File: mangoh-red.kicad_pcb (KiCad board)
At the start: 6 copper layers, 70 x 61.8 mm, 590 parts, among them CN1000 uFL, CN301 uFL, CN302 uFL, CN303 uFL, CN304 USB_A, CN305 USB_B_Micro, CN306 Conn_02x19_Counter_Clockwise, CN307 Conn_02x13_Odd_Even, CN310 Conn_02x03_Odd_Even, CN312 Conn_02x03_Odd_Even, CN400 Conn_02x05_Odd_Even, CN401 Conn_02x05_Odd_Even, CN500 JP036-RT3B4AB, CN801 USB_B_Micro, CN802 Conn_01x02, CN804 Conn_01x03, J200 CF3-Socket, Q312 NSBC114YDP6T5G, Q400 NSBC114YDP6T5G, Q405 NSBC114YDP6T5G, Q600 PDTC115EM, SW401 Conn_02x08_Counter_Clockwise, U1000 MT7697, U1001 MX25L3233FM1I-08G_TR, U1004 SX1509BIULTRT, U1005 TPS61253YFFR, U1006 CP2130-F01-GM, U1007 24AA32AF-I-MNY, U1010 74LVC2G126HD4-7, U1020 74LVC2G126HD4-7, U301 FT230XQ-R, U302 TS3A5018RSVR, U304 74LVC2G126HD4-7, U306 FXMA108BQX, U307 FXMA108BQX, U337 FXMA108BQX, U400 NCP303LSN30T1G, U401 74AUP1G08GM, U402 74AUP1G08GM, U404 TCA9546APWR, U405 74AUP1G08GM, U500 WM8944BECS_R, U501 TS3A5018RSVR, U600 XC6223H29B9R-G, U610 TXS02612ZQSR, U701 USB3503A-1-GL-TR, U702 MIC2026-1YM, U704 BMI160, U705 BMP280, U706 PNJ4K01F, U800 BQ24296RGER, U801 LTC2942IDCB_TRMPBF, U900 TPS7A7300, U901 TPS62420DRC, U903 XC6221A182MR, Y1000 CT2520DB26000C0FZZA1

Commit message: Update
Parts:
- added CN600: CN600, MangOH-Red:CONN_25P_1780x1290_0088CC_MICROSDSIM, B.Cu at (127.6, 74.2)
- added FIL1000: BL1608-05A2450TB, MangOH-Red:FIL_6P_0160x0080_0050CC_MURATA, F.Cu at (203.7, 60.6)
- added L1000: 2.2u, Inductor_SMD:L_0603_1608Metric_Pad1.05x0.95mm_HandSolder, F.Cu at (195.0, 76.7)
- added OSC700: ENE3687A, Crystal:Crystal_SMD_SeikoEpson_FA238V-4Pin_3.2x2.5mm, F.Cu at (211.7, 75.5)
- added SW200: PTS810, Button_Switch_SMD:SW_SPST_PTS810, F.Cu at (212.4, 67.4)
- added SW400: SKTDLDE010, Button_Switch_SMD:SW_SPST_EVQP7A, F.Cu at (196.1, 67.2)
- added SW402: SKTDLDE010, Button_Switch_SMD:SW_SPST_EVQP7A, F.Cu at (202.7, 67.2)
- added U603: ESIM, MangOH-Red:DFN_8P_0500x0600_SLUG_0420x0340_0127CC_ESIM_MODULE_MFF2, F.Cu at (194.4, 60.9)
- SW401: footprint Button_Switch_SMD:SW_DIP_SPSTx08_Slide_6.7x21.88mm_W6.73mm_P2.54mm_LowProfile_JPin -> Button_Switch_SMD:SW_DIP_SPSTx08_Slide_Omron_A6H-8101_W6.15mm_P1.27mm
- U900: footprint Package_DFN_QFN:QFN-20-1EP_5x5mm_P0.65mm_EP3.35x3.35mm -> MangOH-Red:QFN_20P_0500x0500_SLUG_0320x0320_0065CC
- moved D302 147.9 mm to (124.6, 97.8), turned to 90 degrees
- moved L300 143.2 mm to (134.0, 107.0)
- moved TP907 141.5 mm to (146.3, 77.3)
- moved R310 139.7 mm to (134.5, 71.2), turned to 270 degrees
- moved D303 139.7 mm to (134.0, 108.0)
- moved R311 137.1 mm to (135.4, 71.2), turned to 270 degrees
- moved TP261 135.5 mm to (130.2, 93.9)
- moved TP232 134.7 mm to (131.0, 91.2), turned to 270 degrees
- moved D301 132.1 mm to (141.6, 108.0)
- moved TP901 130.2 mm to (156.8, 68.8)
- moved D400 128.5 mm to (125.7, 60.1)
- moved TP906 128.5 mm to (157.7, 76.9)
- moved R506 128.4 mm to (144.6, 57.4), turned to 90 degrees
- moved TP903 128.0 mm to (148.6, 91.1)
- moved TP500 127.2 mm to (160.2, 63.0), turned to 270 degrees
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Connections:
- J200 pad 57: (no net) -> UIM2_RST
- R611 pad 2: (no net) -> Net-(R611-Pad2)
- R645 pad 1: (no net) -> Net-(R645-Pad1)
- U1000 pad 40: (no net) -> Net-(L1000-Pad1)
- U701 pad B3: (no net) -> Net-(OSC700-Pad3)

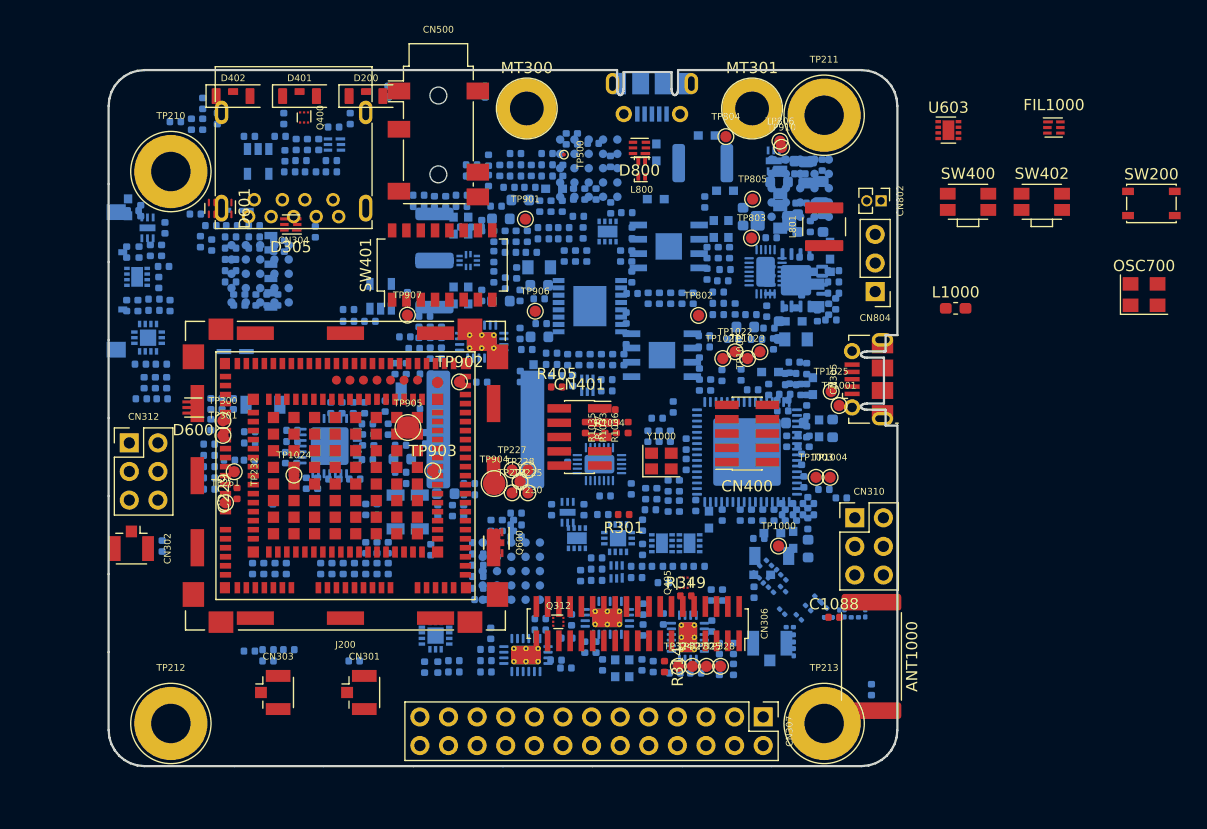
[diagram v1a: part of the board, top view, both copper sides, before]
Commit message: Update models and parts placement
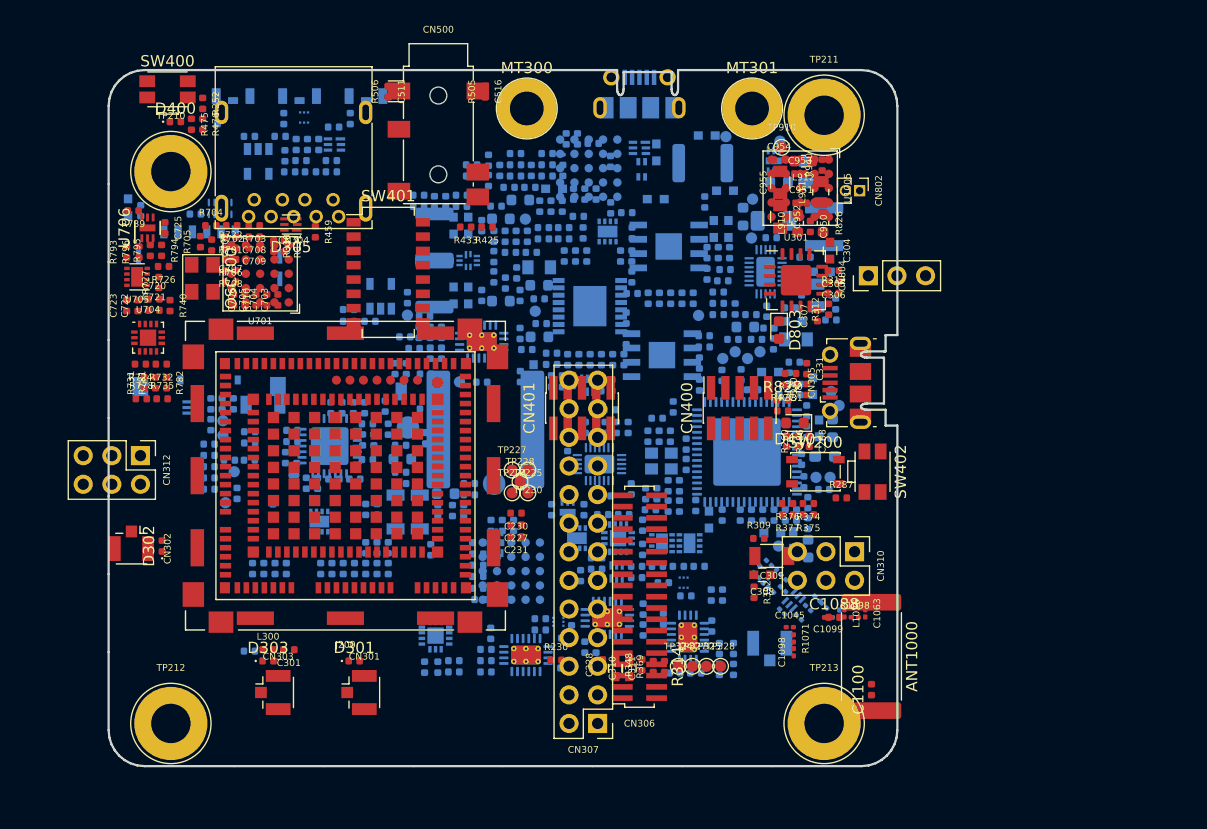
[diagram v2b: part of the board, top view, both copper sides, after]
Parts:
- C1045, C1063, C1098, C1099, C1100, C227, C228, C230, C231, C288, C301, C304, C305, C306, C307, C308, C309, C310, C311, C330, C331, C511, C516, C702, C703, C704, C705, C706, C707, C708, C709, C720, C721, C722, C723, C725, C950, C951, C952, C953, C954, C955, D301, D302, D303, D400, D410, D803, L1026, L300, L910, L911, L912, R1071, R1098, R230, R252, R260, R286, R287, R309, R310, R311, R312, R313, R330, R331, R348, R369, R374, R375, R376, R377, R392, R425, R433, R459, R475, R476, R477, R505, R506, R701, R702, R703, R704, R705, R706, R708, R710, R722, R724, R726, R727, R731, R732, R735, R739, R740, R778, R781, R782, R793, R794, R795, R796, R822, R826, R940, U1005, U301, U701, U704, U705, U706: moved to F.Cu
- C229, D200, D401, D402, D600, D601, D800, FIL1000, L1000, L800, L801, Q312, Q400, Q405, Q600, R1033, R1034, R1035, R1036, R301, R349, R405, R777, TP1000, TP1001, TP1002, TP1003, TP1004, TP1021, TP1022, TP1023, TP1024, TP1025, TP232, TP261, TP300, TP301, TP500, TP802, TP803, TP804, TP805, TP806, TP901, TP902, TP903, TP904, TP905, TP906, TP907, U603, Y1000: moved to B.Cu
- moved OSC700 83.6 mm to (128.1, 74.0), turned to 270 degrees
- moved SW400 71.8 mm to (125.0, 57.2)
- moved U603 65.8 mm to (138.5, 95.6), turned to 90 degrees
- moved FIL1000 47.9 mm to (180.6, 102.6), turned to 45 degrees
- moved SW200 38.2 mm to (182.6, 91.2)
- moved SW402 28.3 mm to (187.6, 91.2), turned to 270 degrees
- moved L1000 17.5 mm to (183.4, 89.8), turned to 180 degrees
- moved CN307 14.7 mm to (163.2, 113.5), turned to 180 degrees
- moved SW401 4.83 mm to (144.6, 73.5), turned to 0 degrees
- moved CN310 3.01 mm to (186.0, 98.3), turned to 270 degrees
- moved CN401 2.58 mm to (161.8, 85.5), turned to 90 degrees
- moved CN600 2.54 mm to (128.7, 76.5), turned to 180 degrees
- moved CN306 2.39 mm to (166.9, 102.3), turned to 180 degrees
- moved CN400 2.35 mm to (175.8, 85.5), turned to 90 degrees
- moved CN802 2.10 mm to (186.5, 66.2)
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
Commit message: Update
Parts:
- moved CN307 14.9 mm to (178.1, 113.3), turned to 270 degrees
- moved ANT1000 6.32 mm to (193.8, 108.0)
- moved CN310 2.46 mm to (185.4, 95.9), turned to 0 degrees
- moved CN802 1.81 mm to (187.8, 65.0), turned to 0 degrees
- moved CN304 1.70 mm to (139.7, 65.3)
- moved CN312 1.60 mm to (121.7, 88.4), turned to 0 degrees
- moved CN306 1.32 mm to (166.1, 103.3), turned to 270 degrees
- moved CN804 0.97 mm to (187.7, 74.6), turned to 180 degrees
- moved SW401 0.60 mm to (145.2, 73.4), turned to 90 degrees
- turned CN600 to 90 degrees

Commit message: Update
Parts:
- CN304: footprint Connector_USB:USB3_A_Molex_48393-001 -> MangOH-Red:CONN_4P_1450x1400_USB_2GND_RA_THRU
- CN306: footprint Connector_PinSocket_1.00mm:PinSocket_2x19_P1.00mm_Vertical_SMD -> MangOH-Red:CONN_38P_1820x1150_0080CC_EVERCLEAR
- CN307: footprint Connector_PinHeader_2.54mm:PinHeader_2x13_P2.54mm_Vertical -> MangOH-Red:CONN_26P_3300x0483_0254CC_HEADER_THRU
- CN310, CN312: footprint Connector_PinHeader_2.54mm:PinHeader_2x03_P2.54mm_Vertical -> MangOH-Red:CONN_6P_0760x0510_HEADER_THRU_0254CC
- CN400, CN401: footprint Connector_PinSocket_1.27mm:PinSocket_2x05_P1.27mm_Vertical_SMD -> MangOH-Red:CONN_10P_0673x0305_0127CC_SMT
- CN801: footprint Connector_USB:USB_Micro-B_Molex-105017-0001 -> MangOH-Red:CONN_5P_0750x0560_USB_5GND_HRS_ZX62RD
- CN802: footprint Connector_PinHeader_1.27mm:PinHeader_1x02_P1.27mm_Vertical -> MangOH-Red:CONN_2P_0590x0450_0200CC_THRU_HEADER
- CN804: footprint Connector_PinHeader_2.54mm:PinHeader_1x03_P2.54mm_Vertical -> MangOH-Red:CONN_3P_0762x0254_VERTICAL_HEADER_SINGLE_ROW_THRU_SAMTEC_TSW
- SW401: footprint Button_Switch_SMD:SW_DIP_SPSTx08_Slide_Omron_A6H-8101_W6.15mm_P1.27mm -> MangOH-Red:SW_16P_1128x0620_0127CC_DIP_SPST
- moved CN307 14.7 mm to (163.4, 113.3), turned to 180 degrees
- moved ANT1000 4.25 mm to (197.8, 106.6)
- moved CN310 2.29 mm to (186.2, 98.0), turned to 270 degrees
- moved CN306 1.61 mm to (167.1, 102.0), turned to 180 degrees
- moved CN312 1.53 mm to (122.8, 89.5), turned to 270 degrees
- moved CN802 1.53 mm to (186.7, 66.0), turned to 270 degrees
- moved CN304 1.48 mm to (139.9, 66.8)
- moved CN804 1.12 mm to (187.4, 73.5), turned to 90 degrees
- moved SW401 0.47 mm to (144.8, 73.2), turned to 0 degrees
- moved C1000 0.29 mm to (168.7, 86.2)
- moved C1006 0.29 mm to (177.2, 83.7)
- moved C1015 0.29 mm to (182.1, 93.7)
- moved C1020 0.29 mm to (178.1, 94.8)
- moved C1021 0.29 mm to (169.7, 94.0)
- moved C1024 0.29 mm to (173.3, 95.2)
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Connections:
- J200 pad 27: (no net) -> UIM1_CLK
- J200 pad 29: (no net) -> UIM1_RESET
- R600 pad 2: (no net) -> Net-(CN600-PadT5)

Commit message: Update
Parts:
- CN305: footprint Connectors_USB:USB_Micro-B_Molex-105017-0001 -> MangOH-Red:CONN_5P_0750x0560_USB_5GND_HRS_ZX62RD
- moved ANT1000 10.2 mm to (187.7, 107.3)
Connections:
- C1100 pad 1: (no net) -> Net-(ANT1000-Pad3)
